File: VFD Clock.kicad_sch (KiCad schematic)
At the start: 0 parts

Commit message: test
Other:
- note added: "Test"
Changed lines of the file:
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@@
 	(generator_version "10.0")
 	(paper "A4")
+	(text "Test"
+		(exclude_from_sim no)
+		(at 104.14 86.106 0)
+		(effects
+			(font
+				(size 1.27 1.27)
+			)
+		)
+	)
 	(sheet_instances
 		(path "/"

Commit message: small updates
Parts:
- added U1, U2, U3, U4, U5, U6: 74HC595, Package_DIP:DIP-16_W7.62mm, symbol 74xx:74HC595
- added U10, U11, U7, U8, U9: UDN2981A, UDN2981A:DIP254P762X533-18, symbol UDN2981A:UDN2981A
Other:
- note removed: "Test"

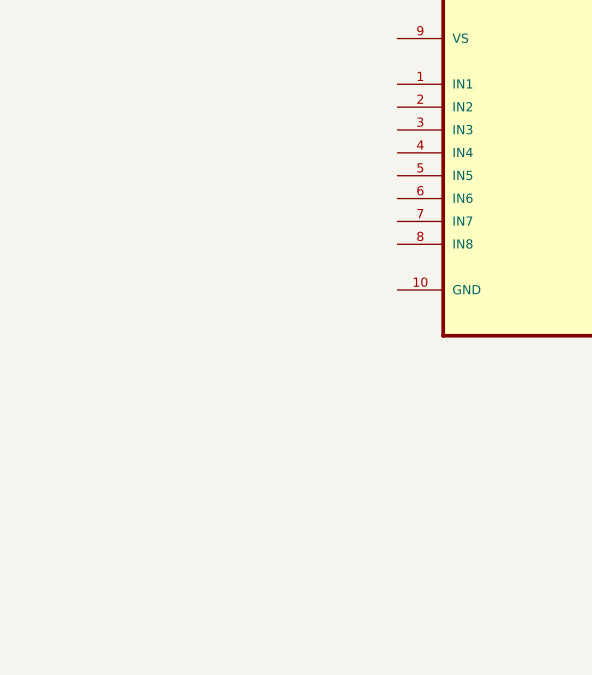
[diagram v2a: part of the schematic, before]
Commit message: added arduino nano
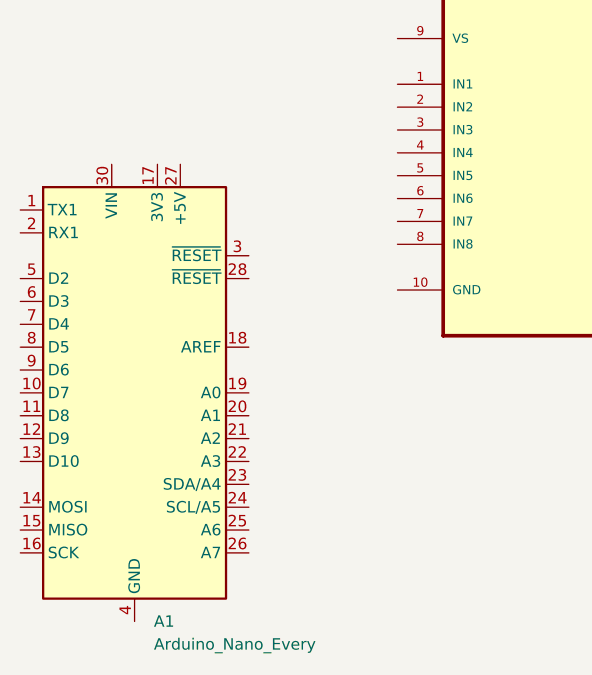
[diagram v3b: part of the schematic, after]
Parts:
- added A1: Arduino_Nano_Every, Module:Arduino_Nano, symbol MCU_Module:Arduino_Nano_Every
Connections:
- new net: A1.29 (GND), A1.4 (GND)
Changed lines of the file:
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@@
+	)
+	(symbol
+		(lib_id "MCU_Module:Arduino_Nano_Every")
+		(at 44.45 153.67 0)
+		(unit 1)
+		(body_style 1)
+		(exclude_from_sim no)
+		(in_bom yes)
+		(on_board yes)
+		(in_pos_files yes)
+		(dnp no)
+		(fields_autoplaced yes)
+		(property "Reference" "A1"
+			(at 46.5933 179.07 0)
+			(show_name no)
+			(do_not_autoplace no)
+			(effects
+				(font
+					(size 1.27 1.27)
+				)
+				(justify left)
+			)
+		)
+		(property "Value" "Arduino_Nano_Every"
+			(at 46.5933 181.61 0)
+			(show_name no)
+			(do_not_autoplace no)
+			(effects
+				(font
+					(size 1.27 1.27)
+				)
+				(justify left)
+			)
+		)
+		(property "Footprint" "Module:Arduino_Nano"
+			(at 44.45 153.67 0)
+			(hide yes)
+			(show_name no)
+			(do_not_autoplace no)
+			(effects
+				(font
+					(size 1.27 1.27)
+					(italic yes)
+				)
+			)
+		)
+		(property "Datasheet" "https://content.arduino.cc/assets/NANOEveryV3.0_sch.pdf"
+			(at 44.45 153.67 0)
+			(hide yes)
+			(show_name no)
+			(do_not_autoplace no)
+			(effects
+				(font
+					(size 1.27 1.27)
+				)
+			)
+		)
+		(property "Description" "Arduino Nano Every"
+			(at 44.45 153.67 0)
+			(hide yes)
+			(show_name no)
+			(do_not_autoplace no)
+			(effects
+				(font
+					(size 1.27 1.27)
+				)
+			)
+		)
+		(pin "10"
+		)
+		(pin "17"
+		)
+		(pin "1"
+		)
+		(pin "4"
+		)
+		(pin "5"
+		)
+		(pin "7"
+		)
+		(pin "3"
+		)
+		(pin "6"
+		)
+		(pin "9"
+		)
+		(pin "11"
+		)
+		(pin "13"
+		)
+		(pin "8"
+		)
+		(pin "15"
+		)
+		(pin "14"
+		)
+		(pin "16"
+		)
+		(pin "2"
+		)
+		(pin "12"
+		)
+		(pin "20"
+		)
+		(pin "23"
+		)
+		(pin "27"
+		)
+		(pin "30"
+		)
+		(pin "25"
+		)
+		(pin "18"
+		)
+		(pin "22"
+		)
+		(pin "19"
+		)
+		(pin "28"
+		)
+		(pin "21"
+		)
+		(pin "24"
+		)
+		(pin "26"
+		)
+		(pin "29"
+		)
+		(instances
+			(project "VFD Clock"
+				(path "/18b1ce2b-a4eb-4908-8bcd-bbd2350e3040"
+					(reference "A1")
+					(unit 1)
+				)
+			)
+		)
 	)
 	(symbol

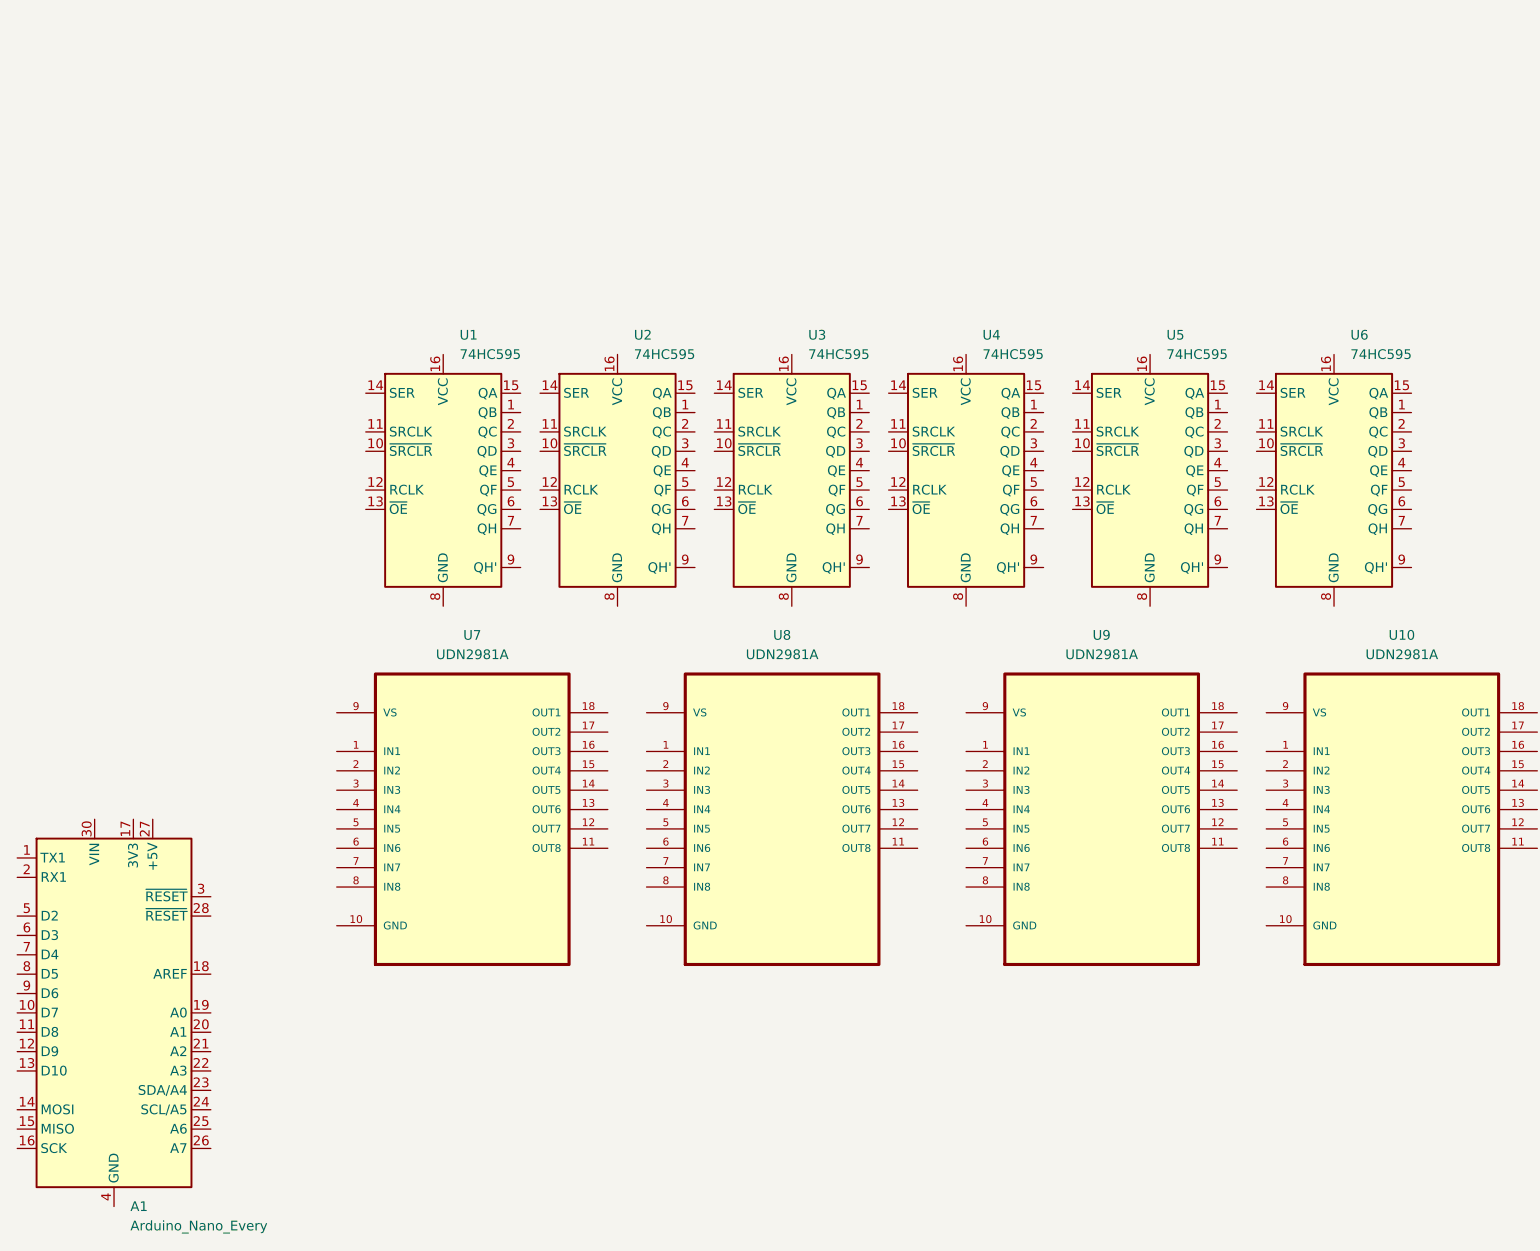
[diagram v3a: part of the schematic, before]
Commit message: created symbol for custom iv-11 part
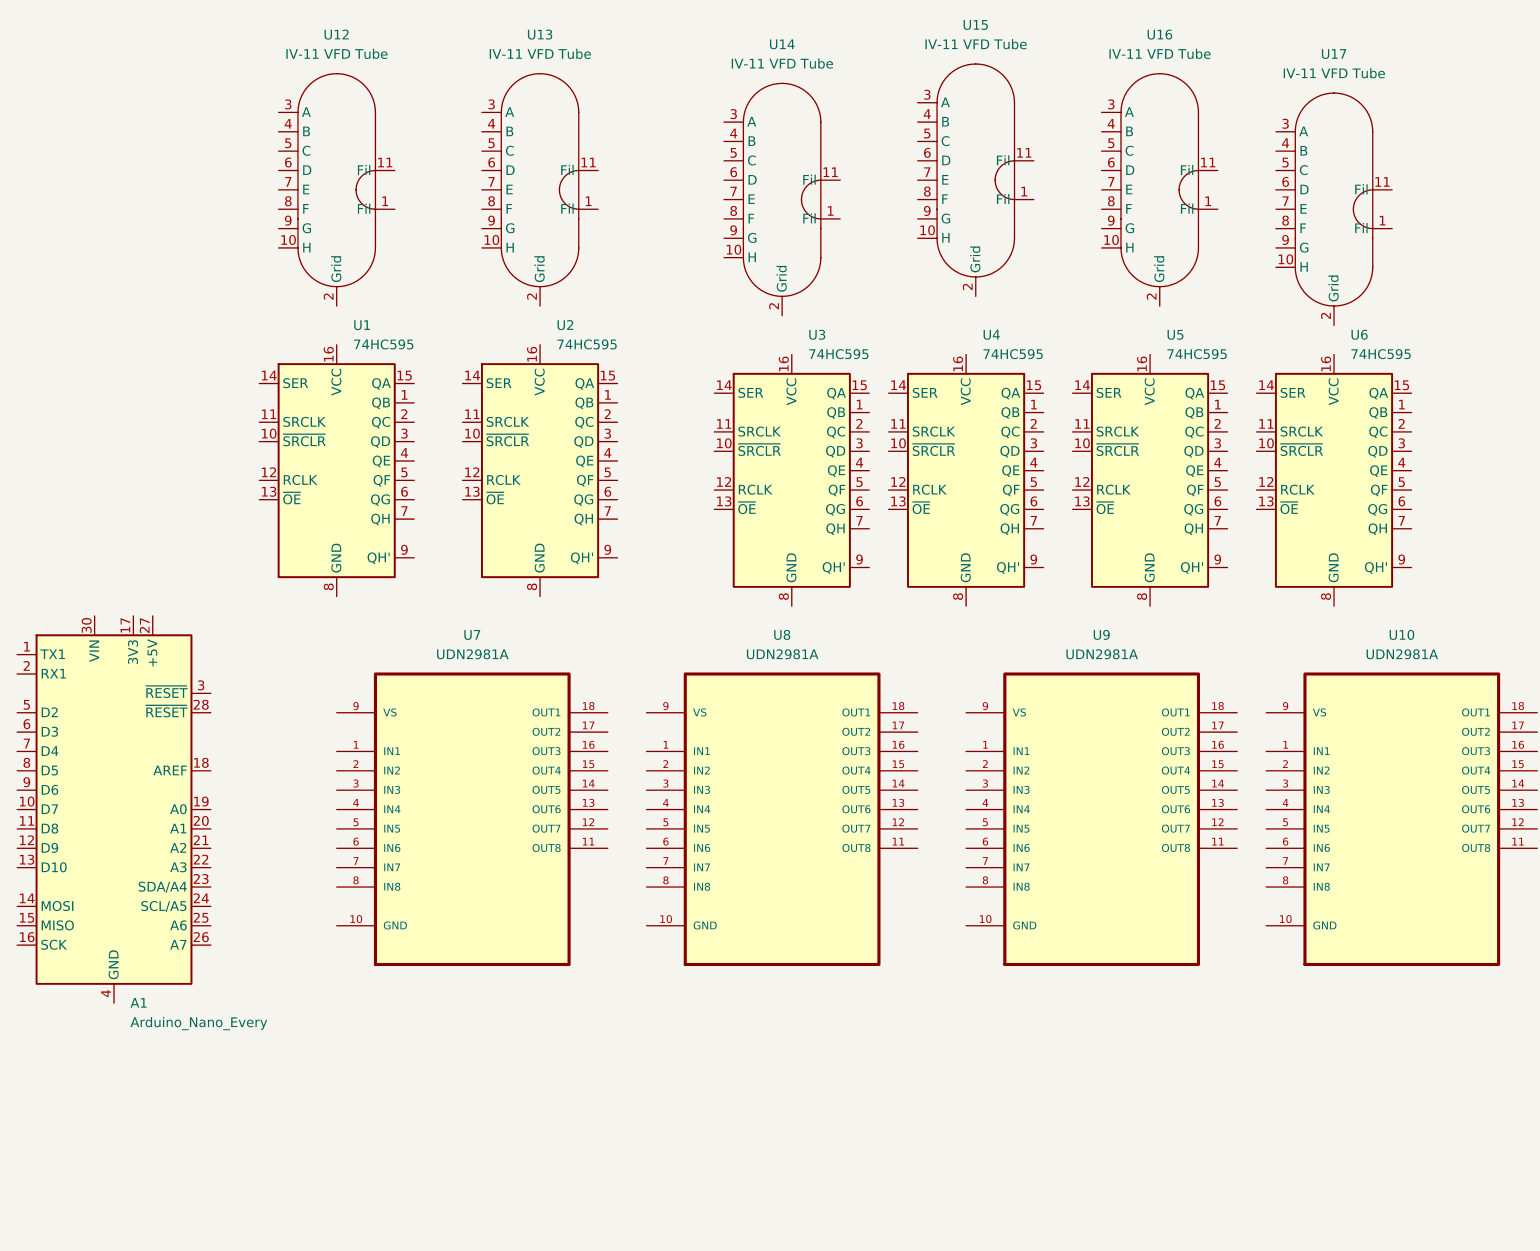
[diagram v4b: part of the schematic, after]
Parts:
- added U12, U13, U14, U15, U16, U17: IV-11 VFD Tube, symbol IV-11 VFD Tube:IV-11_VFD_Tube
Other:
- title: (none) -> IV-11 VFD Clock by Aron Szucs
- moved on the sheet: A1, U1, U2

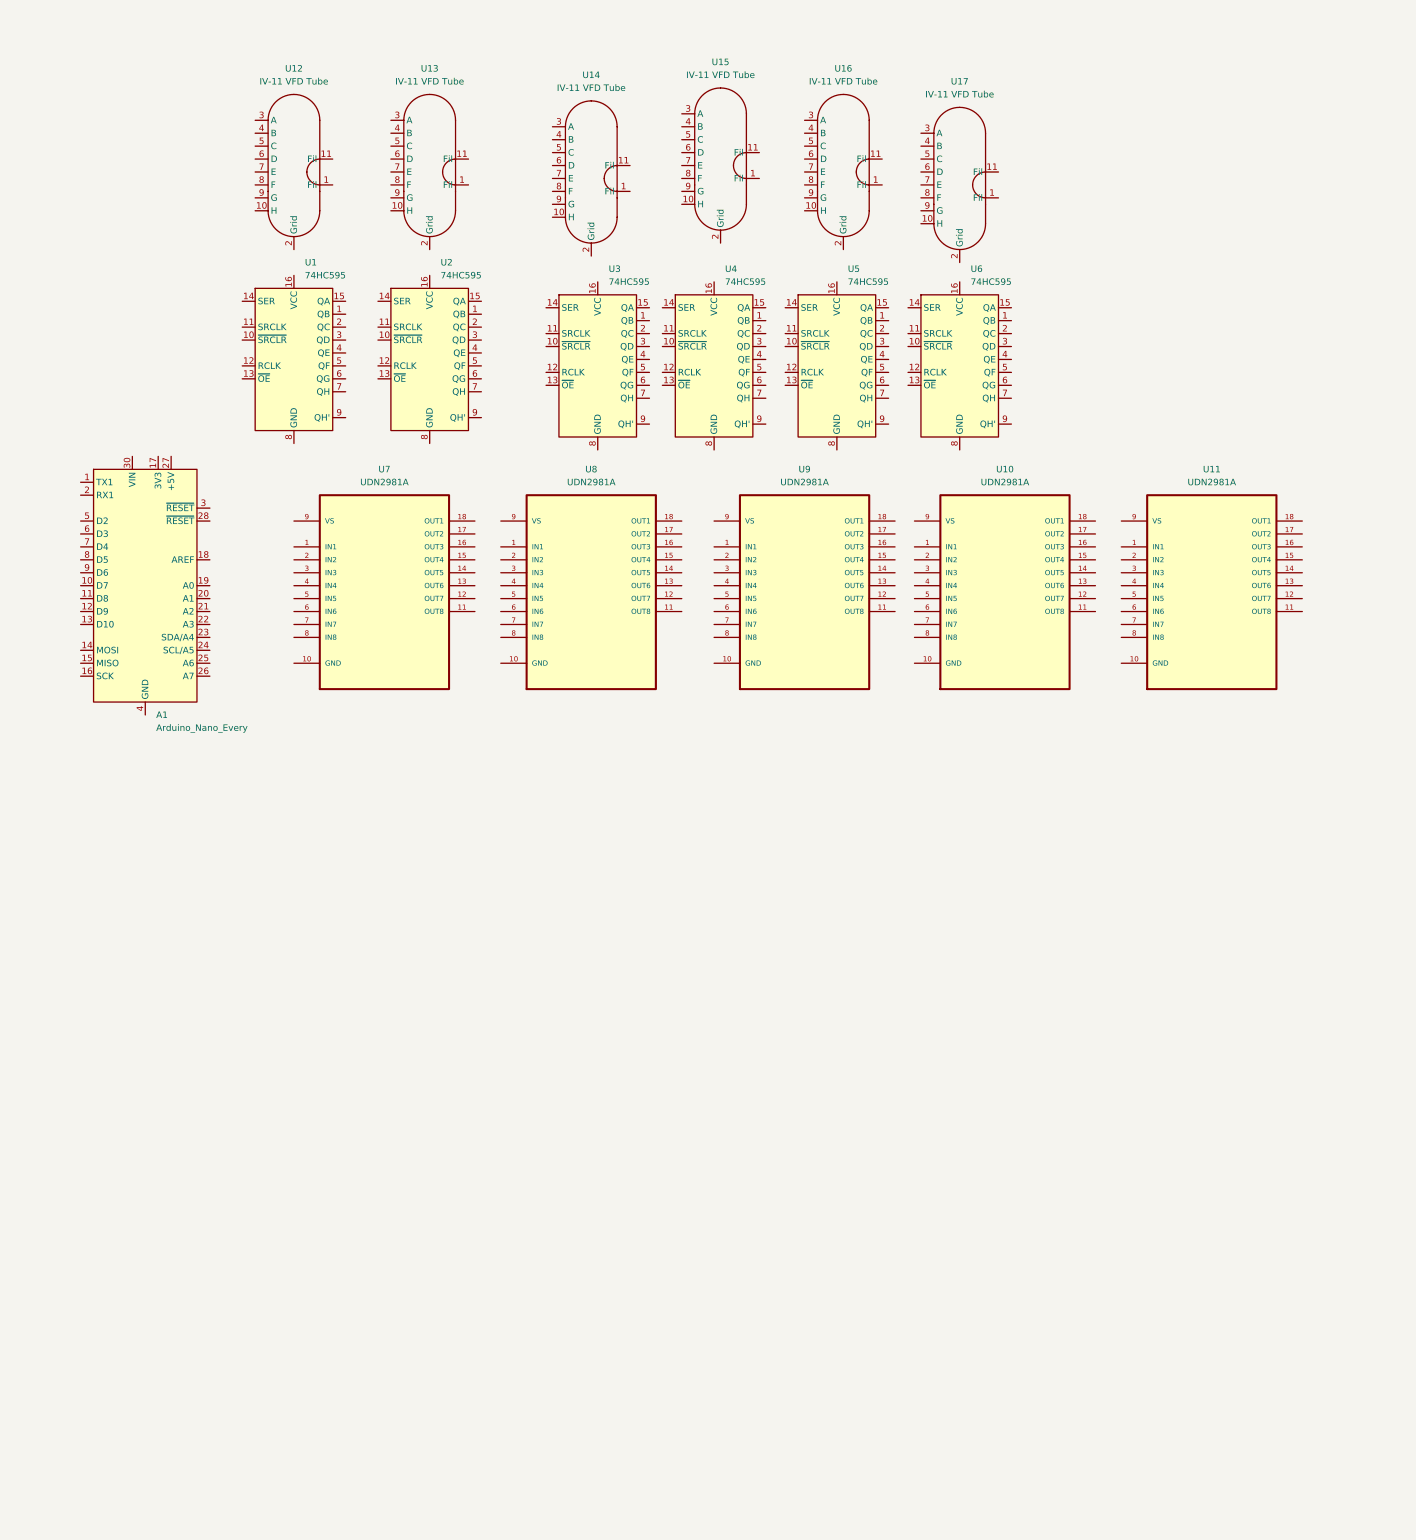
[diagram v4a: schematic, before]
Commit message: fixed symbol/footprint linking, working on schematic
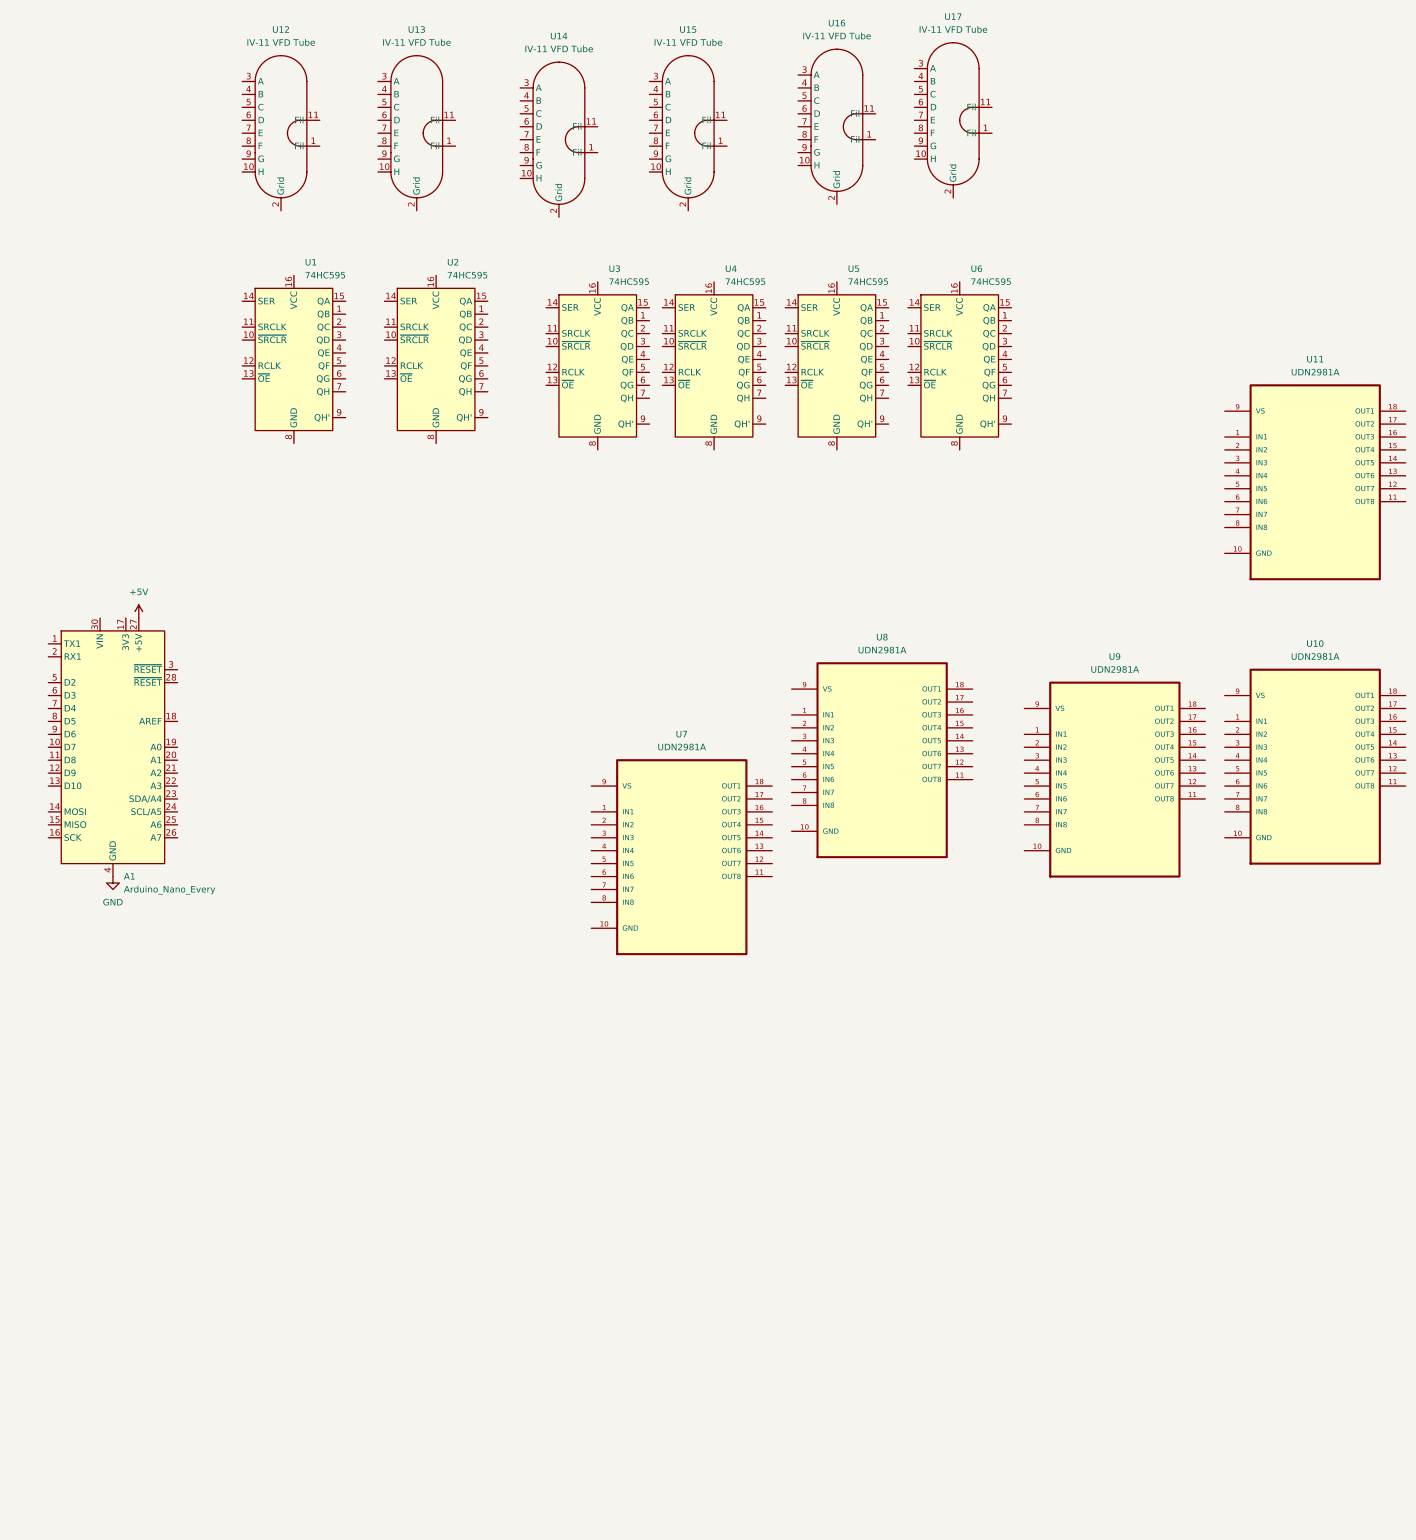
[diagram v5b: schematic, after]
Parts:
- removed U12, U13, U14, U15, U16, U17: IV-11 VFD Tube, symbol IV-11 VFD Tube:IV-11_VFD_Tube
- added U12, U13, U14, U15, U16, U17: IV-11 VFD Tube, Custom Parts:IV-11 VFD Tube, symbol Custom Parts:IV-11_VFD_Tube
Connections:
- net +5V: now reaches A1.27 (+5V)
- net GND: now reaches A1.29 (GND), A1.4 (GND)
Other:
- moved on the sheet: A1, U10, U11, U2, U7, U8, U9

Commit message: progress
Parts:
- removed U10, U11, U8, U9: UDN2981A, UDN2981A:DIP254P762X533-18, symbol UDN2981A:UDN2981A
- removed U13, U14, U15, U16, U17: IV-11 VFD Tube, Custom Parts:IV-11 VFD Tube, symbol Custom Parts:IV-11_VFD_Tube
- removed U2, U3, U4, U5, U6: 74HC595, Package_DIP:DIP-16_W7.62mm, symbol 74xx:74HC595
- renumbered U7 to U2, U12 to U3
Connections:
- net +5V: now also U1.16 (VCC)
- net GND: now also U1.8 (GND), U2.10 (GND), U3.1 (Fil)
- net at U3.10 (H): now also U2.11 (OUT8)
- net +1.5V: now reaches U3.11 (Fil)
- net at U3.3 (A): now also U2.18 (OUT1)
- net at U3.4 (B): now also U2.17 (OUT2)
- net at U3.5 (C): now also U2.16 (OUT3)
- net at U3.6 (D): now also U2.15 (OUT4)
- net at U3.7 (E): now also U2.14 (OUT5)
- net at U3.8 (F): now also U2.13 (OUT6)
- net at U3.9 (G): now also U2.12 (OUT7)
- net at U2.1 (IN1): now also U1.15 (QA)
- net at U2.2 (IN2): now also U1.1 (QB)
- net at U2.3 (IN3): now also U1.2 (QC)
- net at U2.4 (IN4): now also U1.3 (QD)
- net at U2.5 (IN5): now also U1.4 (QE)
- net at U2.6 (IN6): now also U1.5 (QF)
- net at U2.7 (IN7): now also U1.6 (QG)
- net at U2.8 (IN8): now also U1.7 (QH)
- net +25V: now reaches U2.9 (VS)
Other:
- moved on the sheet: U1, U2, U3
